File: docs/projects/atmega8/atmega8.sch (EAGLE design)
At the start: 13 parts, among them IC2 MEGA8-P

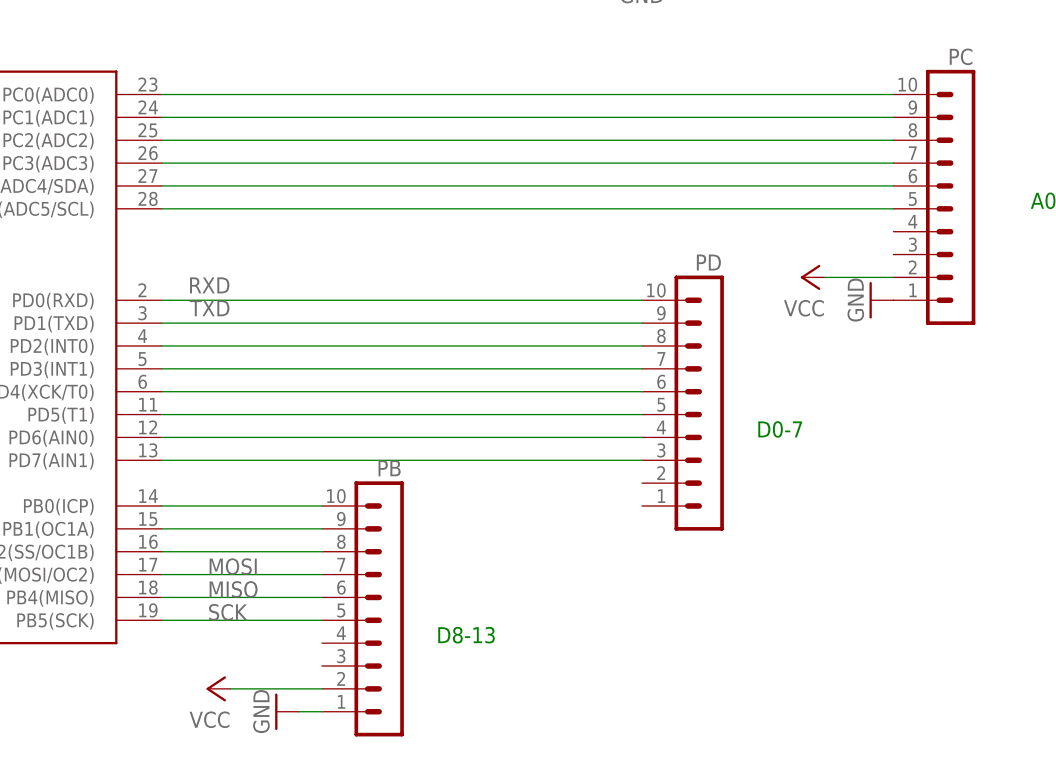
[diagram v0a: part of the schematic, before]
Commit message: atmega8: 6,7 is connected with 14,15 to make I2C compatible with Nucleo
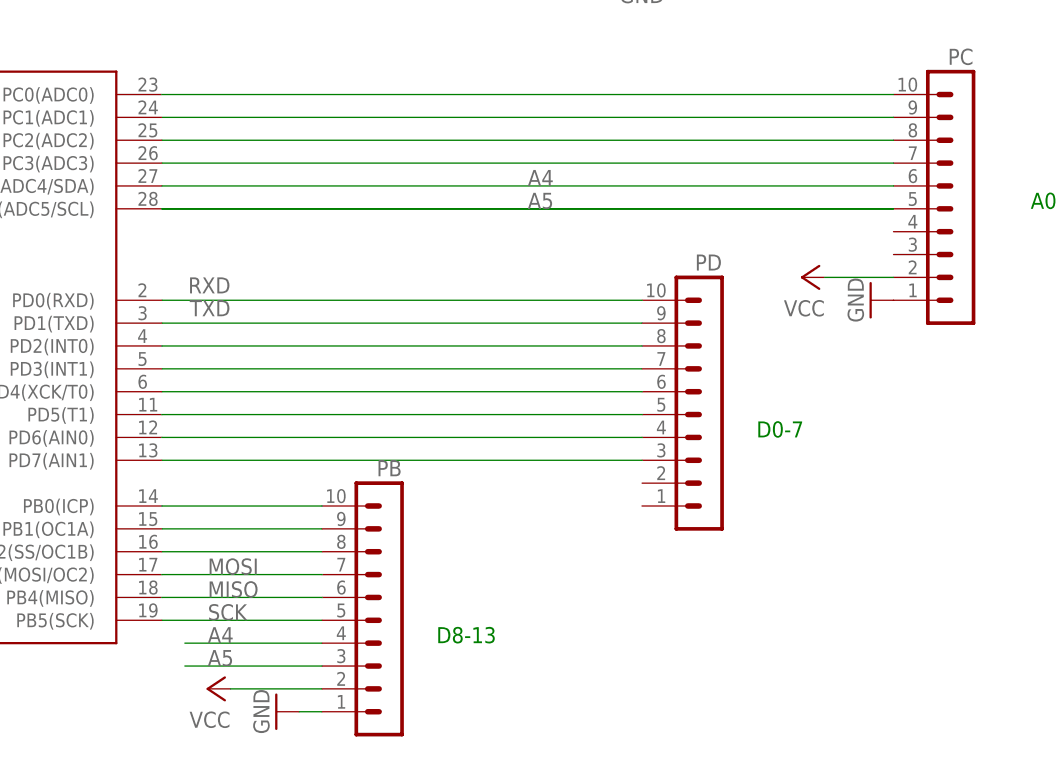
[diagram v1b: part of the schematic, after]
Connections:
- removed net N$7: IC2.PC4(ADC4/SDA), PC.6
- removed net N$8: IC2.PC5(ADC5/SCL), PC.5
- new net A4: IC2.PC4(ADC4/SDA), PB.4, PC.6
- new net A5: IC2.PC5(ADC5/SCL), PB.3, PC.5
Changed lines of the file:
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@@
 <?xml version="1.0" encoding="utf-8"?>
 <!DOCTYPE eagle SYSTEM "eagle.dtd">
-<eagle version="6.2">
+<eagle version="7.4.0">
 <drawing>
 <settings>
@@
 </segment>
 </net>
-<net name="N$7" class="0">
+<net name="A4" class="0">
 <segment>
 <wire x1="177.8" y1="119.38" x2="96.52" y2="119.38" width="0.1524" layer="91"/>
 <pinref part="PC" gate="1" pin="6"/>
 <pinref part="IC2" gate="G$1" pin="PC4(ADC4/SDA)"/>
-</segment>
-</net>
-<net name="N$8" class="0">
+<label x="137.16" y="119.38" size="1.778" layer="95"/>
+</segment>
+<segment>
+<wire x1="114.3" y1="68.58" x2="99.06" y2="68.58" width="0.1524" layer="91"/>
+<pinref part="PB" gate="1" pin="4"/>
+<label x="101.6" y="68.58" size="1.778" layer="95"/>
+</segment>
+</net>
+<net name="A5" class="0">
 <segment>
 <wire x1="177.8" y1="116.84" x2="96.52" y2="116.84" width="0.1524" layer="91"/>
 <pinref part="PC" gate="1" pin="5"/>
 <pinref part="IC2" gate="G$1" pin="PC5(ADC5/SCL)"/>
-</segment>
-</net>
+<label x="137.16" y="116.84" size="1.778" layer="95"/>
+<wire x1="177.8" y1="116.84" x2="96.52" y2="116.84" width="0.1524" layer="91"/>
+</segment>
+<segment>
+<wire x1="114.3" y1="66.04" x2="99.06" y2="66.04" width="0.1524" layer="91"/>
+<pinref part="PB" gate="1" pin="3"/>
+<label x="101.6" y="66.04" size="1.778" layer="95"/>
+</segment>
+</net>
